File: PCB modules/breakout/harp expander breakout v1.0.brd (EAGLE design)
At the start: 72.2 x 42.8 mm, 13 parts, among them SW1 693-1301.9302, SW2 693-1301.9302

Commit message: Corrected silkscreen and minor change to top layer.
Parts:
- removed SW2: 693-1301.9302, SparkFun-Electromechanical:TACTILE-PTH
- added SW0: 693-1301.9302, SparkFun-Electromechanical:TACTILE-PTH
- moved SW1 33.0 mm to (52.6, 20.1)
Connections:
- net GND: now also SW0.4; no longer SW2.4
- net N$14: now also SW1.2; no longer SW2.2
- net N$24: now also SW0.2; no longer SW1.2
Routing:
- net +5V: track 74.1 -> 72.4 mm
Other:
- board text added: "5"
- board text added: "6"
- board text added: "7"
- board text added: "8"
- board text added: "9"
- board text removed: "IO5"
- board text removed: "IO6"
- board text removed: "IO7"
- board text removed: "IO8"
- board text removed: "IO9"

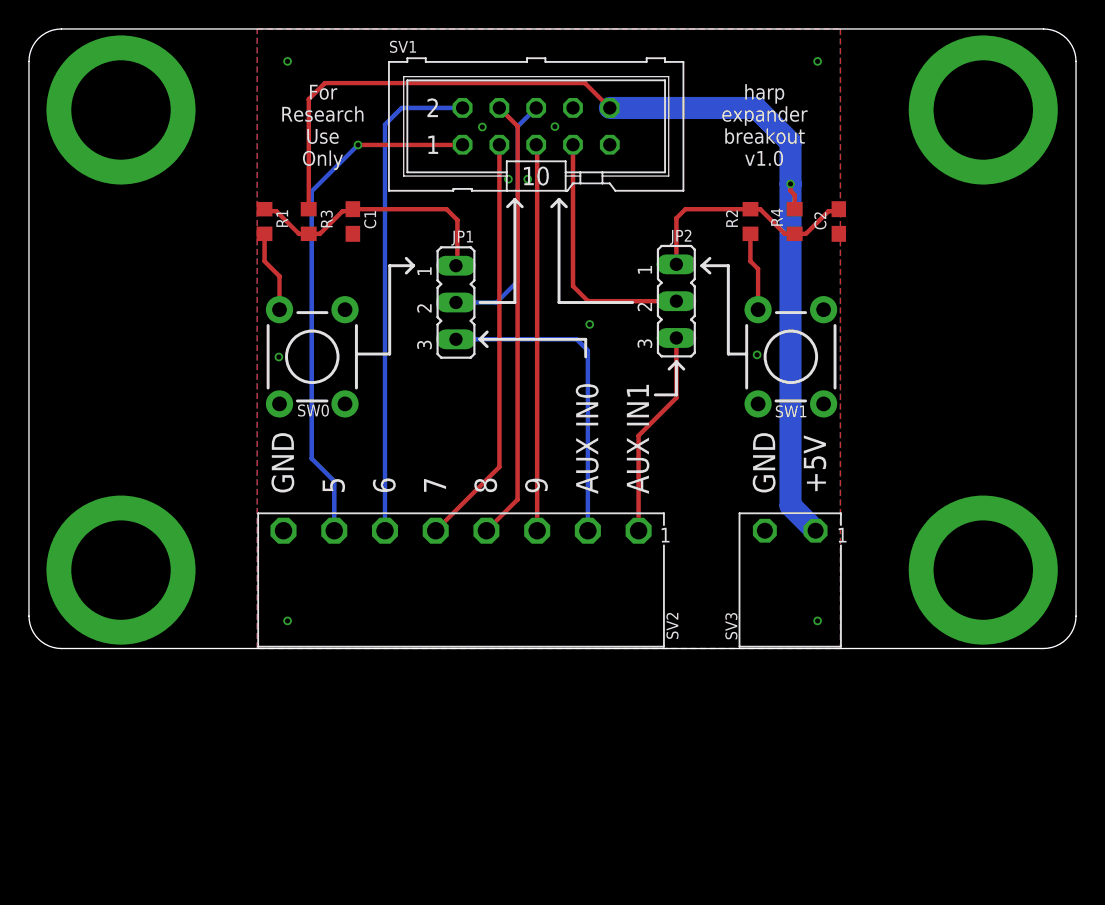
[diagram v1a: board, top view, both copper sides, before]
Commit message: Corrected wrong buttons polarity.
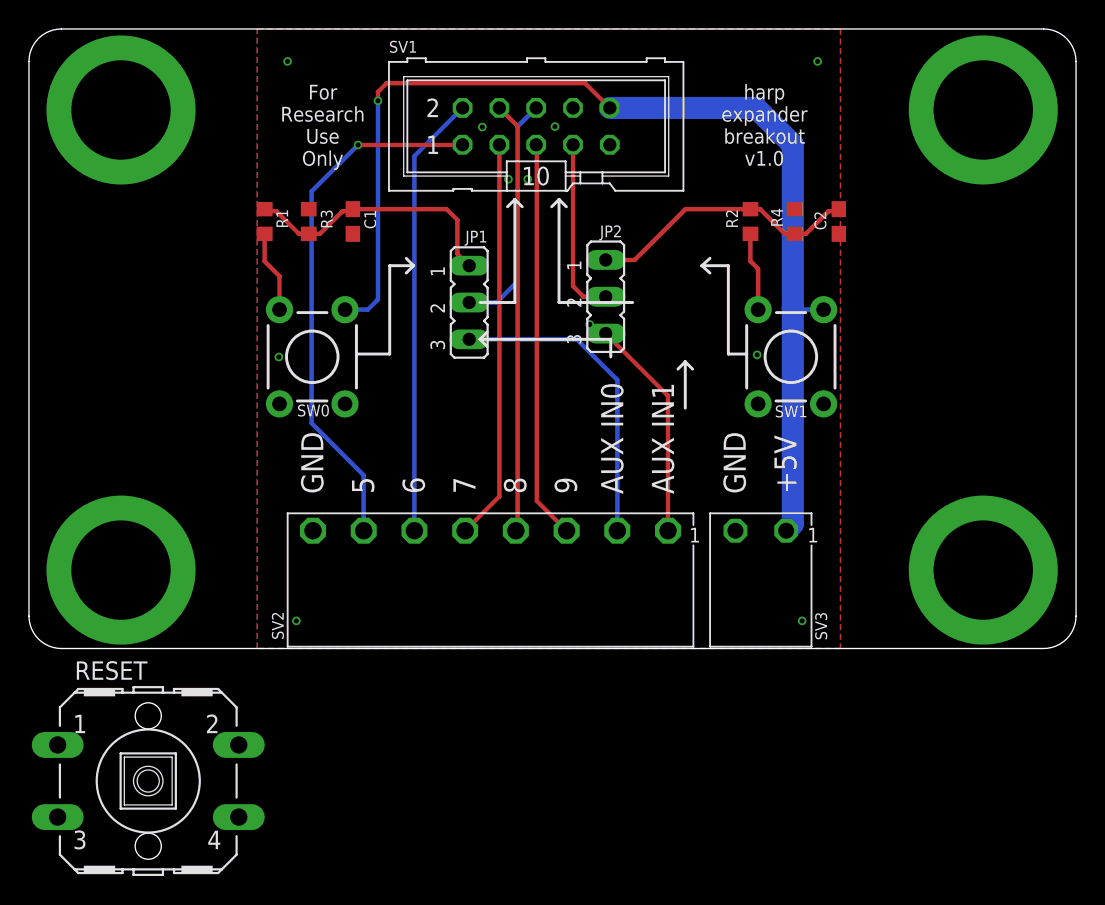
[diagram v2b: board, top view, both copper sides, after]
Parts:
- added RESET: (no value), switch-omron:B3F-40XX
- C1, C2: value 4.7uF -> 1uF
- R1, R2: value 270 -> 2.2k
- R3, R4: value 2.7k -> 4.3k
- moved JP2 4.89 mm to (39.8, 24.3)
- moved SV3 2.03 mm to (50.2, 8.13)
- moved SV2 2.03 mm to (31.8, 8.13)
- moved JP1 0.91 mm to (30.4, 23.9)
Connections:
- net +5V: now also SW0.4, SW1.4; no longer R3.1, R4.1
- net GND: now also R3.1, R4.1; no longer SW0.4, SW1.4
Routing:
- net AUX_IN1: track 17.3 -> 12.3 mm
- net +5V: track 72.4 -> 76.5 mm
- net IO6: track 33.9 -> 30.6 mm
- net N$16: track 16.1 -> 18.9 mm
- net AUX_IN1_CONNECTOR: track 14.4 -> 15.4 mm
- net AUX_IN0: track 17.4 -> 16.4 mm
- net IO9: track 26.7 -> 27.5 mm
- net IO8: track 30.6 -> 29.7 mm
- net IO7: track 28.5 -> 27.6 mm
- net IO5: track 35.8 -> 36.7 mm

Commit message: Updated files for final revision before production.
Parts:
- removed RESET: (no value), switch-omron:B3F-40XX
- SW0, SW1: value 693-1301.9302 -> (none); device SparkFun-Electromechanical:TACTILE-PTH -> switch-omron:B3F-40XX
- moved C2 3.06 mm to (55.6, 32.5), turned to 90 degrees
- moved R2 3.06 mm to (49.5, 32.5)
- moved R4 3.06 mm to (52.5, 32.5)
- moved C1 3.05 mm to (22.4, 32.5)
- moved R1 3.05 mm to (16.3, 32.5)
- moved R3 3.05 mm to (19.3, 32.5)
- moved SW0 2.45 mm to (19.2, 22.6)
- moved SW1 2.43 mm to (52.4, 22.6)
- moved JP2 1.83 mm to (41.6, 24.3)
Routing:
- net +5V: track 76.5 -> 71.4 mm
- net N$24: track 5.66 -> 3.05 mm
- net N$14: track 5.45 -> 3.05 mm
- net AUX_IN1: track 12.3 -> 14.1 mm
- net N$16: track 18.9 -> 17.4 mm
- net N$25: track 18.5 -> 19.8 mm
- net AUX_IN1_CONNECTOR: track 15.4 -> 14.6 mm

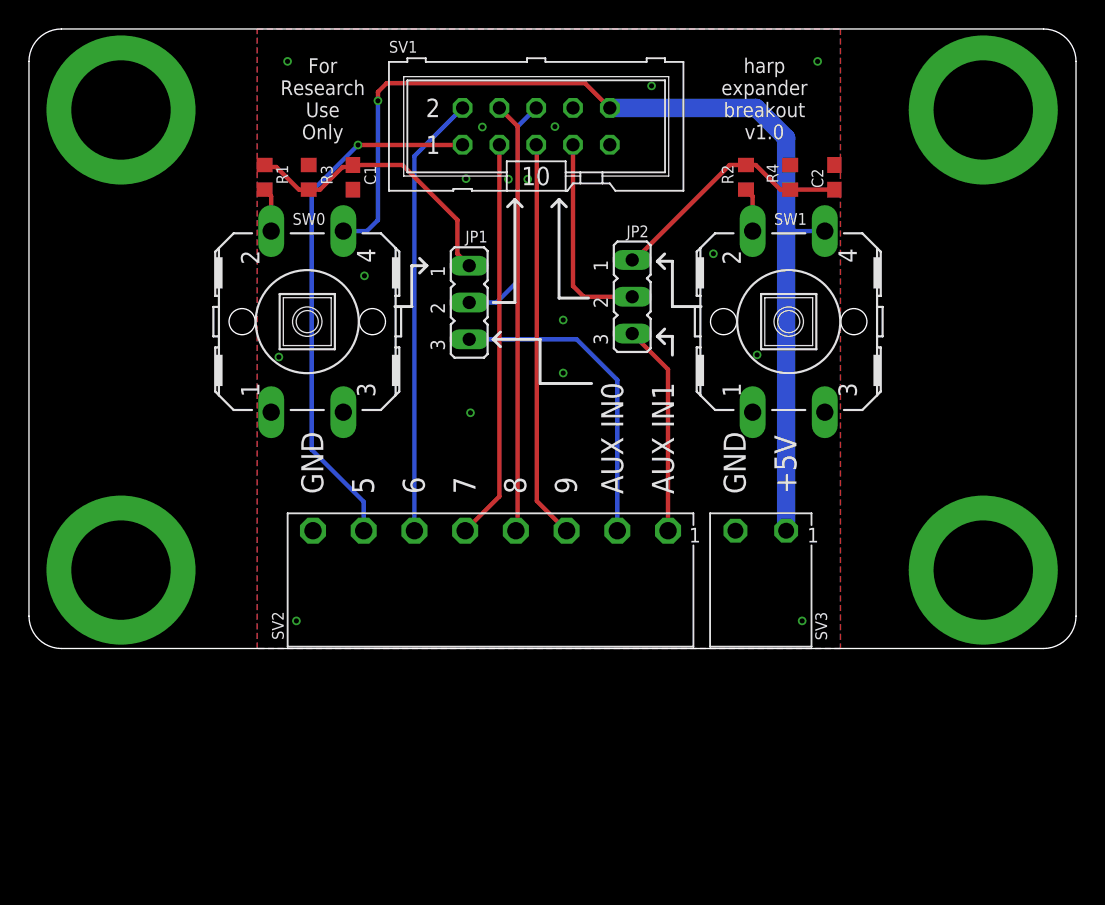
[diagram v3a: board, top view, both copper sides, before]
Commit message: Increased distance between screw connectors.
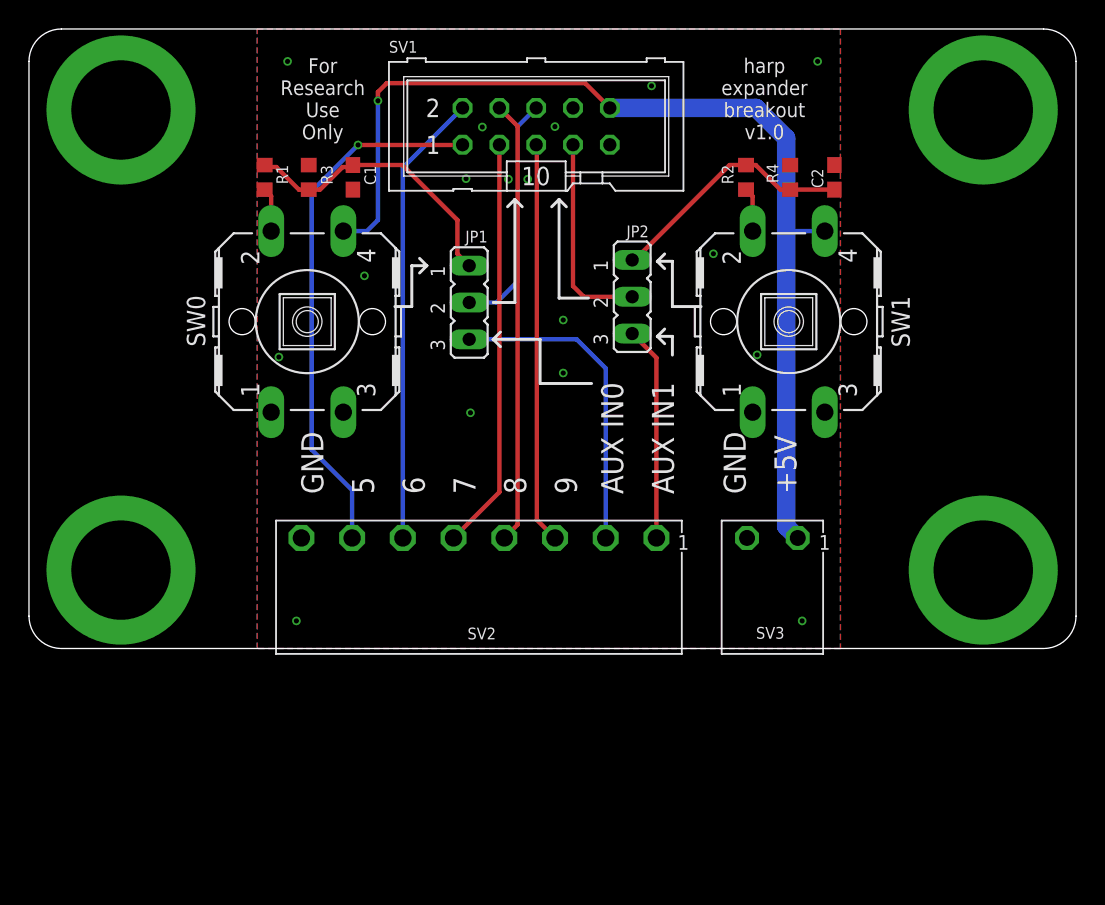
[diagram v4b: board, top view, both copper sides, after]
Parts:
- moved SV3 0.94 mm to (51.0, 7.63)
- moved SV2 0.94 mm to (31.0, 7.63)
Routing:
- net IO7: track 27.6 -> 28.4 mm
- net IO6: track 30.6 -> 31.4 mm
- net IO8: track 29.7 -> 30.6 mm
- net +5V: track 71.4 -> 72.2 mm
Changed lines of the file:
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@@
 <setting verticaltext="up"/>
 </settings>
-<grid distance="12" unitdist="mil" unit="mil" style="lines" multiple="1" display="yes" altdistance="4" altunitdist="mil" altunit="mil"/>
+<grid distance="19.6850394" unitdist="mil" unit="mil" style="lines" multiple="1" display="yes" altdistance="4" altunitdist="mil" altunit="mil"/>
 <layers>
 <layer number="1" name="Top" color="4" fill="1" visible="yes" active="yes"/>
@@
 <attribute name="VALUE" x="35" y="41.112" size="1.778" layer="27" ratio="10"/>
 </element>
-<element name="SV2" library="CNP-connectors" package="CON_3.5MM_1X8" value="CON_3.5MM_1X8" x="31.848" y="8.128" smashed="yes" rot="R180">
-<attribute name="NAME" x="16.7692" y="2.5568" size="0.8128" layer="25" font="vector" ratio="15" rot="R270"/>
-<attribute name="VALUE" x="45.813" y="12.009" size="1.27" layer="27" ratio="10" rot="R180"/>
-</element>
-<element name="SV3" library="CNP-connectors" package="CON_3.5MM_1X2" value="CON_3.5MM_1X2" x="50.1585" y="8.128" smashed="yes" rot="R180">
-<attribute name="NAME" x="54.2596" y="2.5285" size="0.8128" layer="25" font="vector" ratio="15" rot="R270"/>
-<attribute name="VALUE" x="53.9635" y="12.009" size="1.27" layer="27" ratio="10" rot="R180"/>
+<element name="SV2" library="CNP-connectors" package="CON_3.5MM_1X8" value="CON_3.5MM_1X8" x="31.048" y="7.628" smashed="yes" rot="R180">
+<attribute name="NAME" x="30.26" y="0.6276" size="0.8128" layer="25" font="vector" ratio="15"/>
+<attribute name="VALUE" x="45.013" y="11.509" size="1.27" layer="27" ratio="10" rot="R180"/>
+</element>
+<element name="SV3" library="CNP-connectors" package="CON_3.5MM_1X2" value="CON_3.5MM_1X2" x="50.9585" y="7.628" smashed="yes" rot="R180">
+<attribute name="NAME" x="50.1699" y="0.6724" size="0.8128" layer="25" font="vector" ratio="15"/>
+<attribute name="VALUE" x="54.7635" y="11.509" size="1.27" layer="27" ratio="10" rot="R180"/>
 </element>
 <element name="R2" library="rcl" package="R0603" value="2.2k" x="49.4792" y="32.512" smashed="yes" rot="R270">
@@
 <attribute name="MF" value="OMRON COMPONENTS USA" x="19.2024" y="22.5552" size="1.778" layer="27" rot="R90" display="off"/>
 <attribute name="MPN" value="B3F-4000" x="19.2024" y="22.5552" size="1.778" layer="27" rot="R90" display="off"/>
-<attribute name="NAME" x="18.1864" y="29.2354" size="0.8128" layer="25" font="vector" ratio="15"/>
+<attribute name="NAME" x="12.163" y="22.6008" size="1.27" layer="25" font="vector" ratio="15" rot="R90" align="bottom-center"/>
 <attribute name="OC_FARNELL" value="176434" x="19.2024" y="22.5552" size="1.778" layer="27" rot="R90" display="off"/>
 <attribute name="OC_NEWARK" value="36K3105" x="19.2024" y="22.5552" size="1.778" layer="27" rot="R90" display="off"/>
@@
 <attribute name="MF" value="OMRON COMPONENTS USA" x="52.4256" y="22.5552" size="1.778" layer="27" rot="R90" display="off"/>
 <attribute name="MPN" value="B3F-4000" x="52.4256" y="22.5552" size="1.778" layer="27" rot="R90" display="off"/>
-<attribute name="NAME" x="51.4096" y="29.2354" size="0.8128" layer="25" font="vector" ratio="15"/>
+<attribute name="NAME" x="60.7822" y="22.5552" size="1.27" layer="25" font="vector" ratio="15" rot="R90" align="bottom-center"/>
 <attribute name="OC_FARNELL" value="176434" x="52.4256" y="22.5552" size="1.778" layer="27" rot="R90" display="off"/>
 <attribute name="OC_NEWARK" value="36K3105" x="52.4256" y="22.5552" size="1.778" layer="27" rot="R90" display="off"/>
@@
 <contactref element="SV3" pad="P1"/>
 <wire x1="50.1756" y1="37.302" x2="40.08" y2="37.302" width="1.27" layer="16"/>
-<wire x1="52.2485" y1="8.128" x2="52.2478" y2="8.1287" width="1.27" layer="16"/>
+<wire x1="53.0485" y1="7.628" x2="52.2478" y2="8.4287" width="1.27" layer="16"/>
 <wire x1="40.08" y1="37.302" x2="38.3676" y2="39.0144" width="0.3048" layer="1"/>
 <wire x1="38.3676" y1="39.0144" x2="24.6888" y2="39.0144" width="0.3048" layer="1"/>
@@
 <contactref element="SW1" pad="4"/>
 <wire x1="52.2478" y1="35.2298" x2="50.1756" y2="37.302" width="1.27" layer="16"/>
-<wire x1="52.2478" y1="8.1287" x2="52.2478" y2="28.6512" width="1.27" layer="16"/>
-<wire x1="52.2478" y1="28.6512" x2="52.2478" y2="31.6992" width="1.27" layer="16"/>
-<wire x1="52.2478" y1="31.6992" x2="52.2478" y2="35.2298" width="1.27" layer="16"/>
+<wire x1="52.2478" y1="8.4287" x2="52.2478" y2="28.6512" width="1.27" layer="16"/>
+<wire x1="52.2478" y1="28.6512" x2="52.2478" y2="35.2298" width="1.27" layer="16"/>
 <wire x1="54.9148" y1="28.8036" x2="52.4002" y2="28.8036" width="0.3048" layer="16"/>
 <wire x1="52.4002" y1="28.8036" x2="52.2478" y2="28.6512" width="0.3048" layer="16"/>
@@
 <contactref element="SV1" pad="1"/>
 <contactref element="SV2" pad="P7"/>
-<wire x1="23.098" y1="8.128" x2="23.098" y2="10.1252" width="0.3048" layer="16"/>
-<wire x1="23.098" y1="10.1252" x2="19.5072" y2="13.716" width="0.3048" layer="16"/>
+<wire x1="22.298" y1="7.628" x2="22.298" y2="10.9252" width="0.3048" layer="16"/>
+<wire x1="22.298" y1="10.9252" x2="19.5072" y2="13.716" width="0.3048" layer="16"/>
 <wire x1="19.5072" y1="13.716" x2="19.5072" y2="31.5468" width="0.3048" layer="16"/>
 <wire x1="19.5072" y1="31.5468" x2="22.7076" y2="34.7472" width="0.3048" layer="16"/>
@@
 <contactref element="SV1" pad="2"/>
 <contactref element="SV2" pad="P6"/>
-<wire x1="26.598" y1="8.128" x2="26.598" y2="33.98" width="0.3048" layer="16"/>
-<wire x1="26.598" y1="33.98" x2="29.92" y2="37.302" width="0.3048" layer="16"/>
+<wire x1="25.798" y1="7.628" x2="25.798" y2="33.18" width="0.3048" layer="16"/>
+<wire x1="25.798" y1="33.18" x2="29.92" y2="37.302" width="0.3048" layer="16"/>
 </signal>
 <signal name="IO7">
 <contactref element="SV1" pad="3"/>
 <contactref element="SV2" pad="P5"/>
-<wire x1="30.098" y1="8.128" x2="32.46" y2="10.49" width="0.3048" layer="1"/>
-<wire x1="32.46" y1="10.49" x2="32.46" y2="34.762" width="0.3048" layer="1"/>
+<wire x1="29.298" y1="7.628" x2="32.46" y2="10.79" width="0.3048" layer="1"/>
+<wire x1="32.46" y1="10.79" x2="32.46" y2="34.762" width="0.3048" layer="1"/>
 </signal>
 <signal name="IO8">
 <contactref element="SV1" pad="4"/>
 <contactref element="SV2" pad="P4"/>
-<wire x1="33.7185" y1="8.2485" x2="33.598" y2="8.128" width="0.3048" layer="1"/>
+<wire x1="33.7185" y1="8.5485" x2="32.798" y2="7.628" width="0.3048" layer="1"/>
 <wire x1="33.7185" y1="36.0435" x2="32.46" y2="37.302" width="0.3048" layer="1"/>
-<wire x1="33.7185" y1="8.2485" x2="33.7185" y2="36.0435" width="0.3048" layer="1"/>
+<wire x1="33.7185" y1="8.5485" x2="33.7185" y2="36.0435" width="0.3048" layer="1"/>
 </signal>
 <signal name="IO9">
 <contactref element="SV1" pad="5"/>
 <contactref element="SV2" pad="P3"/>
-<wire x1="35.0406" y1="34.7468" x2="35.0406" y2="10.1854" width="0.3048" layer="1"/>
-<wire x1="37.098" y1="8.128" x2="35.0406" y2="10.1854" width="0.3048" layer="1"/>
+<wire x1="35.0406" y1="34.7468" x2="35.0406" y2="8.8854" width="0.3048" layer="1"/>
+<wire x1="36.298" y1="7.628" x2="35.0406" y2="8.8854" width="0.3048" layer="1"/>
 <wire x1="35.0406" y1="34.7468" x2="35.0254" y2="34.762" width="0.3048" layer="1"/>
 <wire x1="35.0254" y1="34.762" x2="35" y2="34.762" width="0.3048" layer="1"/>
@@
 <contactref element="SV2" pad="P2"/>
 <contactref element="JP1" pad="3"/>
-<wire x1="40.598" y1="8.128" x2="40.598" y2="18.5332" width="0.3048" layer="16"/>
-<wire x1="40.598" y1="18.5332" x2="37.7952" y2="21.336" width="0.3048" layer="16"/>
+<wire x1="39.798" y1="7.628" x2="39.798" y2="19.3332" width="0.3048" layer="16"/>
+<wire x1="39.798" y1="19.3332" x2="37.7952" y2="21.336" width="0.3048" layer="16"/>
 <wire x1="37.7952" y1="21.336" x2="30.3784" y2="21.336" width="0.3048" layer="16"/>
 </signal>
@@
 <contactref element="SV2" pad="P1"/>
 <contactref element="JP2" pad="3"/>
-<wire x1="41.6256" y1="21.7328" x2="44.098" y2="19.2604" width="0.3048" layer="1"/>
-<wire x1="44.098" y1="19.2604" x2="44.098" y2="8.128" width="0.3048" layer="1"/>
+<wire x1="41.6256" y1="21.7328" x2="43.298" y2="20.0604" width="0.3048" layer="1"/>
+<wire x1="43.298" y1="20.0604" x2="43.298" y2="7.628" width="0.3048" layer="1"/>
 </signal>
 <signal name="S$1">
